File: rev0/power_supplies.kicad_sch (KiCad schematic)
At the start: 50 parts, among them IC1 ECP5-BGA256, U1 AP2171WG-7, U12 AP2171WG-7, U13 AP2171WG-7, U3 AP7366-33W5-7, U4 TCR2EF115, U5 MIC5504-2.5YM5

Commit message: hardware: use DNP field for DNP notation
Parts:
- TP28, TP29, TP3, TP30, TP31, TP4, TP5: DNP (none) -> DNP; Note DNP -> (none)
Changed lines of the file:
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@@
       (effects (font (size 1.27 1.27)) hide)
     )
-    (property "Note" "DNP" (id 4) (at 77.47 99.06 0)
+    (property "DNP" "DNP" (id 4) (at 77.47 99.06 0)
       (effects (font (size 1.27 1.27)) hide)
     )
@@
       (effects (font (size 1.27 1.27)) hide)
     )
-    (property "Note" "DNP" (id 4) (at 152.4 97.79 0)
+    (property "DNP" "DNP" (id 4) (at 152.4 97.79 0)
       (effects (font (size 1.27 1.27)) hide)
     )
@@
       (effects (font (size 1.27 1.27)) hide)
     )
-    (property "Note" "DNP" (id 4) (at 152.4 153.67 0)
+    (property "DNP" "DNP" (id 4) (at 152.4 153.67 0)
       (effects (font (size 1.27 1.27)) hide)
     )
@@
       (effects (font (size 1.27 1.27)) hide)
     )
-    (property "Note" "DNP" (id 4) (at 73.66 182.88 0)
+    (property "DNP" "DNP" (id 4) (at 73.66 182.88 0)
       (effects (font (size 1.27 1.27)) hide)
     )
@@
       (effects (font (size 1.27 1.27)) hide)
     )
-    (property "Note" "DNP" (id 4) (at 48.26 182.88 0)
+    (property "DNP" "DNP" (id 4) (at 48.26 182.88 0)
       (effects (font (size 1.27 1.27)) hide)
     )
@@
       (effects (font (size 1.27 1.27)) hide)
     )
-    (property "Note" "DNP" (id 4) (at 41.91 152.4 0)
+    (property "DNP" "DNP" (id 4) (at 41.91 152.4 0)
       (effects (font (size 1.27 1.27)) hide)
     )
@@
       (effects (font (size 1.27 1.27)) hide)
     )
-    (property "Note" "DNP" (id 4) (at 58.42 152.4 0)
-      (effects (font (size 1.27 1.27)) hide)
-    )
+    (property "DNP" "DNP" (id 4) (at 58.42 152.4 0)
+      (effects (font (size 1.27 1.27)) hide)
+    )

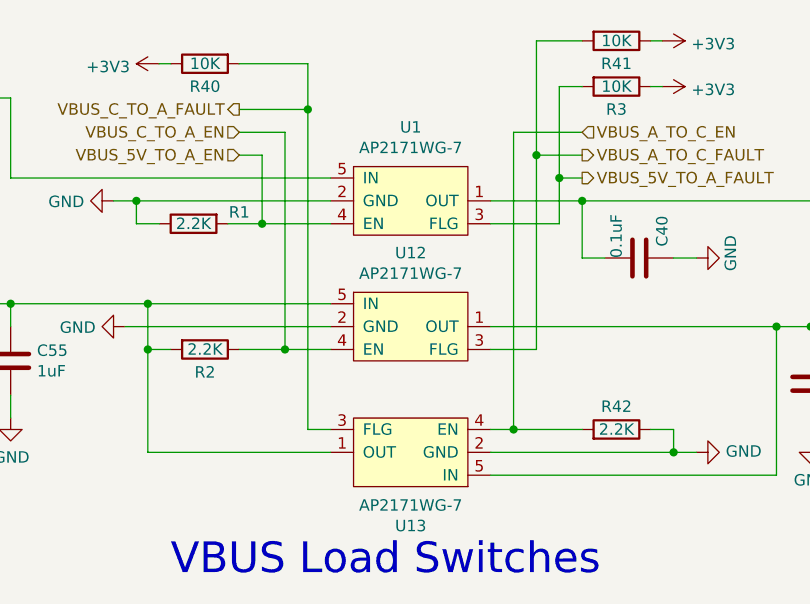
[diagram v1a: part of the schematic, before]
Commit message: hardware: consistently use lowercase k for kilo
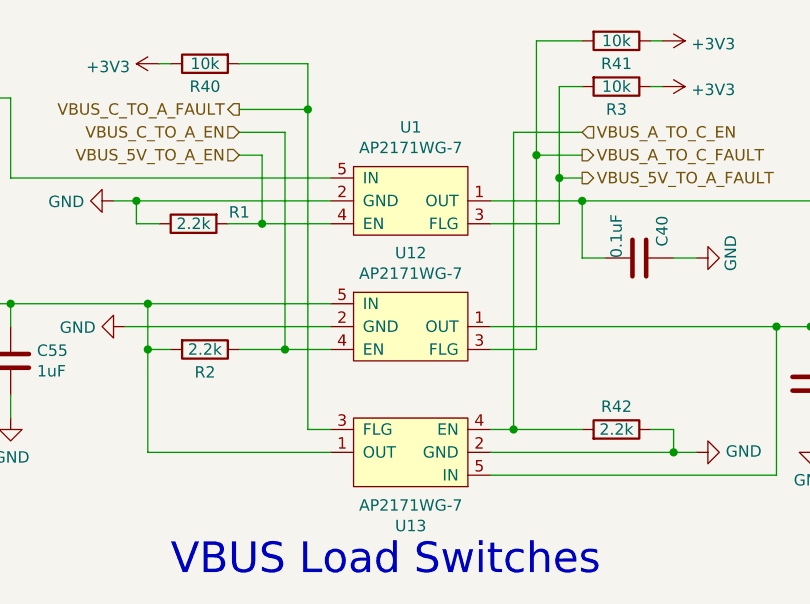
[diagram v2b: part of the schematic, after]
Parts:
- R1, R2, R42: value 2.2K -> 2.2k
- R3, R40, R41: value 10K -> 10k
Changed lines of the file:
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@@
     (in_bom yes) (on_board yes)
     (property "Reference" "R2" (id 0) (at 184.15 52.07 90))
-    (property "Value" "2.2K" (id 1) (at 184.15 49.53 90))
+    (property "Value" "2.2k" (id 1) (at 184.15 49.53 90))
     (property "Footprint" "Resistor_SMD:R_0402_1005Metric" (id 2) (at 184.15 47.752 90)
       (effects (font (size 1.27 1.27)) hide)
@@
     (in_bom yes) (on_board yes)
     (property "Reference" "R1" (id 0) (at 187.96 34.29 90))
-    (property "Value" "2.2K" (id 1) (at 182.88 35.56 90))
+    (property "Value" "2.2k" (id 1) (at 182.88 35.56 90))
     (property "Footprint" "Resistor_SMD:R_0402_1005Metric" (id 2) (at 182.88 33.782 90)
       (effects (font (size 1.27 1.27)) hide)
@@
     (in_bom yes) (on_board yes)
     (property "Reference" "R42" (id 0) (at 229.87 55.88 90))
-    (property "Value" "2.2K" (id 1) (at 229.87 58.42 90))
+    (property "Value" "2.2k" (id 1) (at 229.87 58.42 90))
     (property "Footprint" "Resistor_SMD:R_0402_1005Metric" (id 2) (at 229.87 60.198 90)
       (effects (font (size 1.27 1.27)) hide)
@@
     (in_bom yes) (on_board yes)
     (property "Reference" "R3" (id 0) (at 229.87 22.86 90))
-    (property "Value" "10K" (id 1) (at 229.87 20.32 90))
+    (property "Value" "10k" (id 1) (at 229.87 20.32 90))
     (property "Footprint" "Resistor_SMD:R_0402_1005Metric" (id 2) (at 229.87 18.542 90)
       (effects (font (size 1.27 1.27)) hide)
@@
     (in_bom yes) (on_board yes)
     (property "Reference" "R41" (id 0) (at 229.87 17.78 90))
-    (property "Value" "10K" (id 1) (at 229.87 15.24 90))
+    (property "Value" "10k" (id 1) (at 229.87 15.24 90))
     (property "Footprint" "Resistor_SMD:R_0402_1005Metric" (id 2) (at 229.87 13.462 90)
       (effects (font (size 1.27 1.27)) hide)
@@
     (in_bom yes) (on_board yes)
     (property "Reference" "R40" (id 0) (at 184.15 20.32 90))
-    (property "Value" "10K" (id 1) (at 184.15 17.78 90))
+    (property "Value" "10k" (id 1) (at 184.15 17.78 90))
     (property "Footprint" "Resistor_SMD:R_0402_1005Metric" (id 2) (at 184.15 16.002 90)
       (effects (font (size 1.27 1.27)) hide)

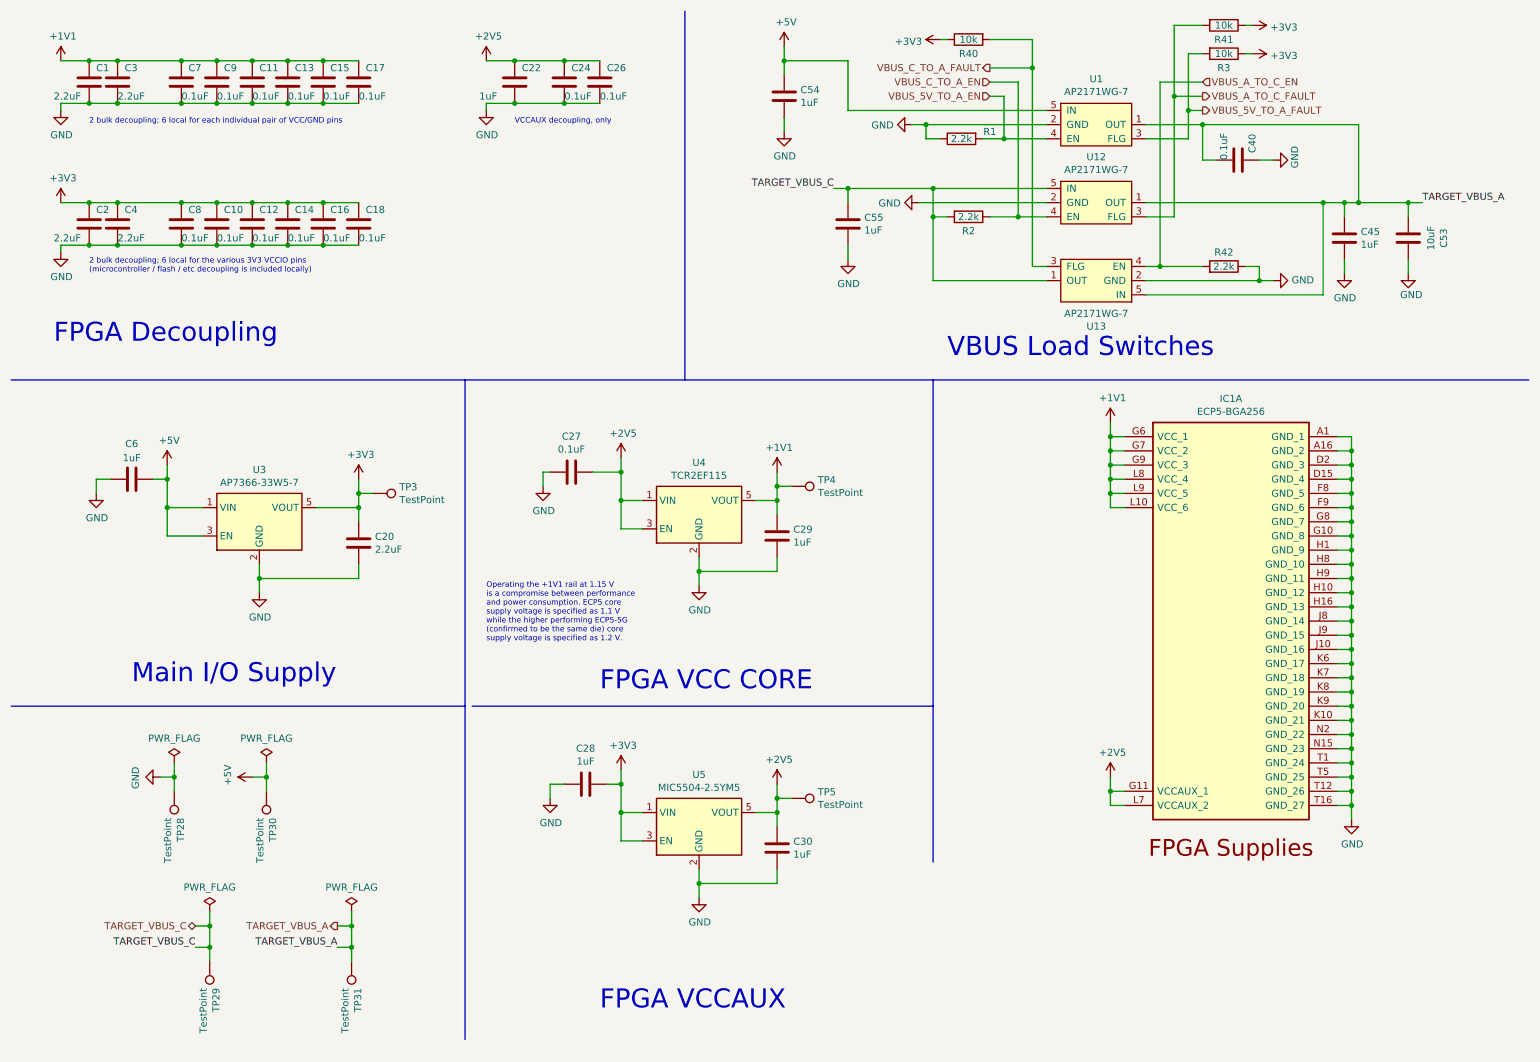
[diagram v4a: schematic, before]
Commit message: hardware: restore 1.8 V RAM supply as an option
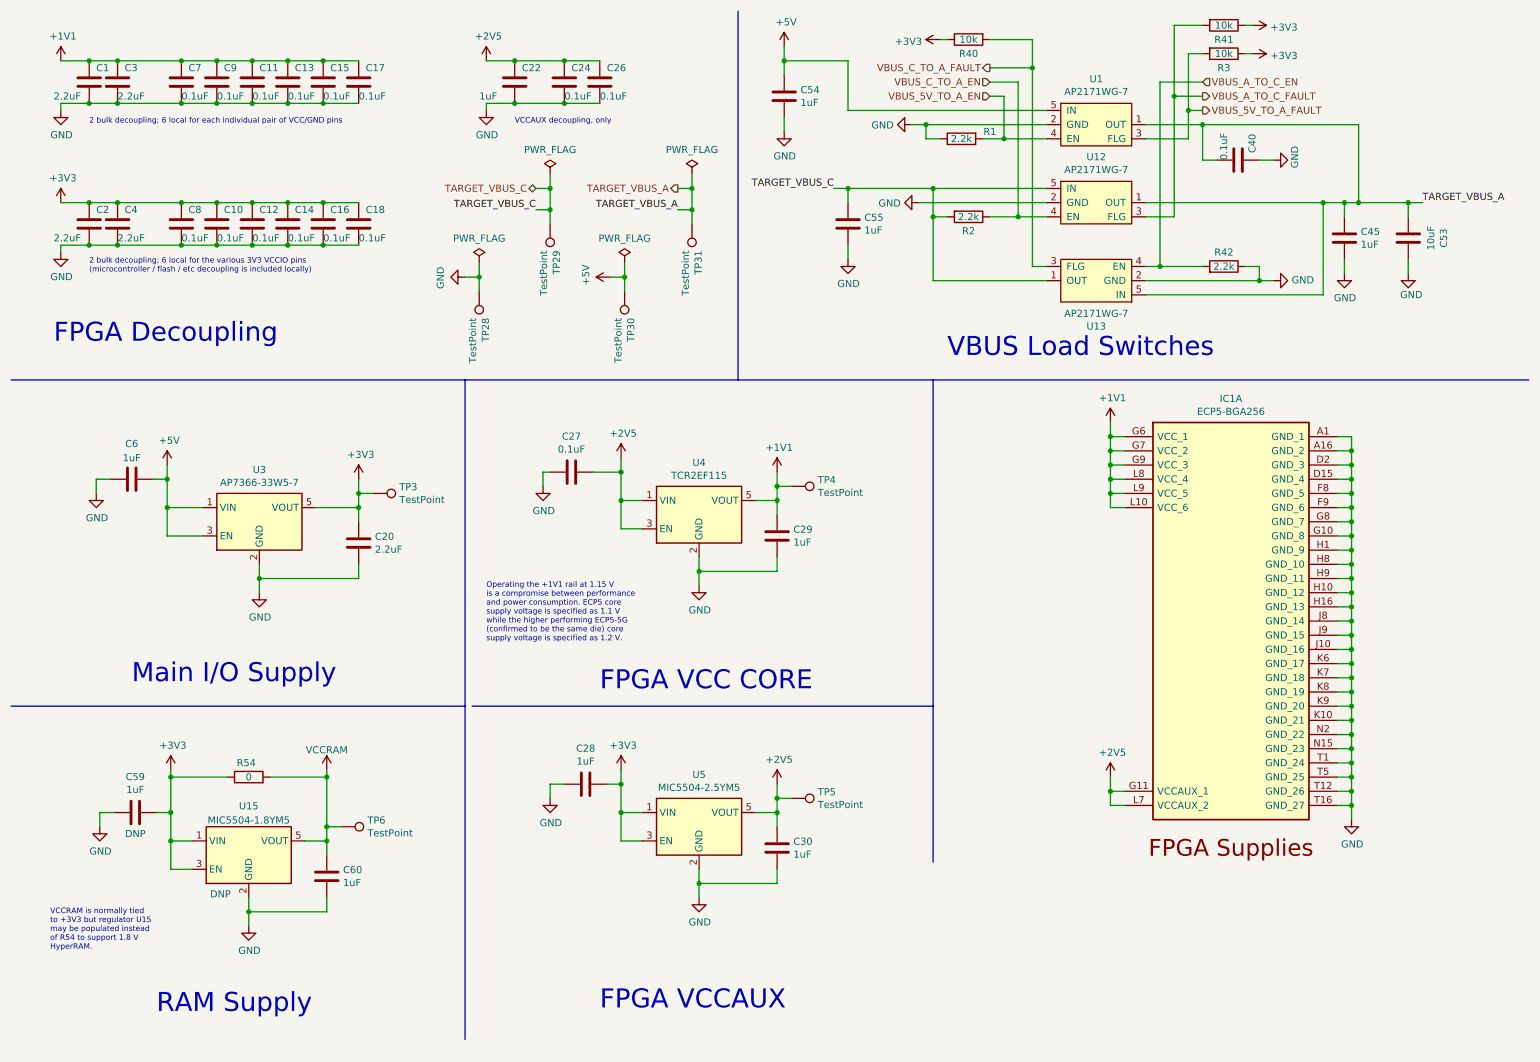
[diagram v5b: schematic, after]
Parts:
- added C59, C60: 1uF, Capacitor_SMD:C_0603_1608Metric, symbol Device:C
- added R54: 0, Resistor_SMD:R_0402_1005Metric, symbol Device:R
- added TP6: TestPoint, TestPoint:TestPoint_Pad_D1.0mm, symbol Connector:TestPoint
- added U15: MIC5504-1.8YM5, Package_TO_SOT_SMD:SOT-23-5, symbol Regulator_Linear:MIC5504-1.8YM5
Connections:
- net +3V3: now also C59.1, R54.1, U15.1 (VIN), U15.3 (EN)
- net GND: now also C59.2, C60.2, U15.2 (GND)
- new net VCCRAM: C60.1, R54.2, TP6.1, U15.5 (VOUT)
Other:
- note added: "RAM Supply"
- note added: "VCCRAM is normally tied to +3V3 but regulator U15 may be populated instead of R54 to support 1.8 V HyperRAM."
- moved on the sheet: TP28, TP29, TP30, TP31

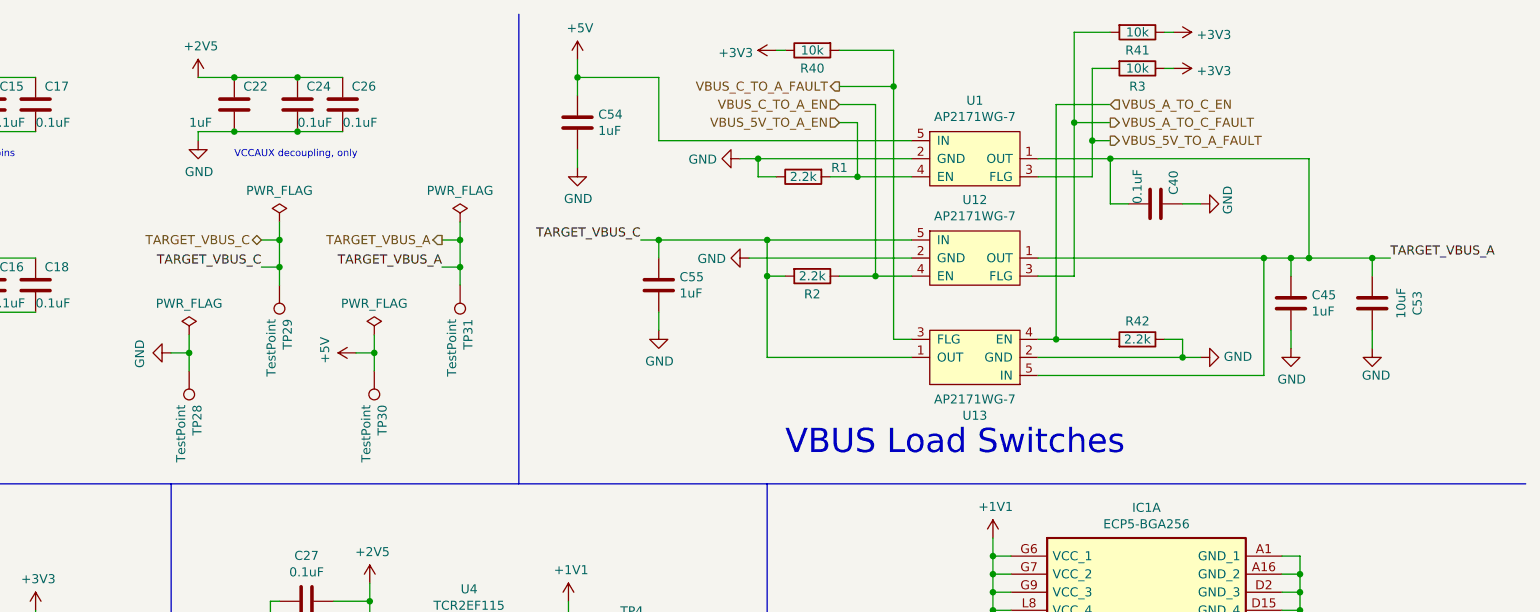
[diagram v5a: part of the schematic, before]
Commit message: hardware: replace VBUS pass-through switches
- increase maximum voltage with discrete FET solution
- pass through Control and Aux VBUS directly, not +5V supply rail
- add current sense resistors
- eliminate discharge current of previous power switches
- eliminate possible overvoltage condition of previous power switches
- remove 10 uF VBUS output capacitor C53
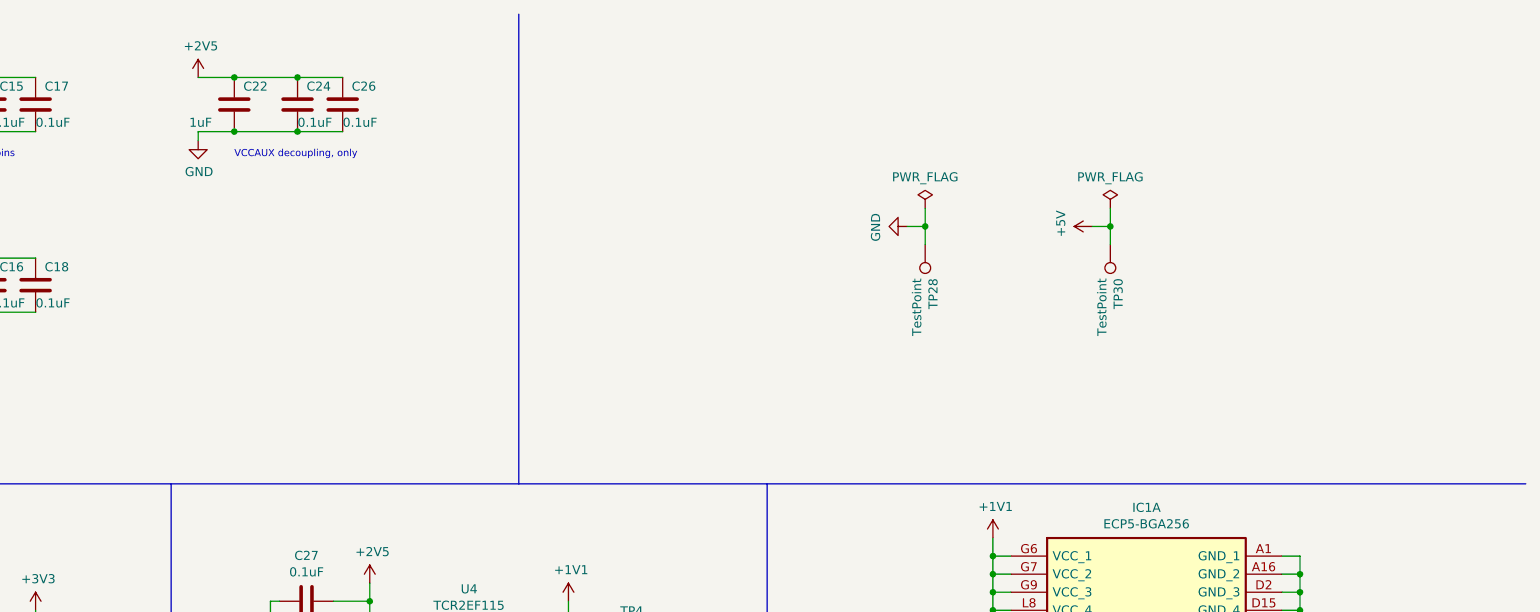
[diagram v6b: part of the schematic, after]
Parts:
- removed C40: 0.1uF, Capacitor_SMD:C_0402_1005Metric, symbol Device:C
- removed C45, C54, C55: 1uF, Capacitor_SMD:C_0603_1608Metric, symbol Device:C
- removed C53: 10uF, Capacitor_SMD:C_0805_2012Metric, symbol Device:C
- removed R1, R2, R42: 2.2k, Resistor_SMD:R_0402_1005Metric, symbol Device:R
- removed R3, R40, R41: 10k, Resistor_SMD:R_0402_1005Metric, symbol Device:R
- removed TP29, TP31: TestPoint, TestPoint:TestPoint_Pad_D1.0mm, symbol Connector:TestPoint
- removed U1, U12, U13: AP2171WG-7, Package_TO_SOT_SMD:SOT-23-5, symbol support_hardware:AP22804-SOT
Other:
- note removed: "VBUS Load Switches"
- moved on the sheet: TP28, TP30

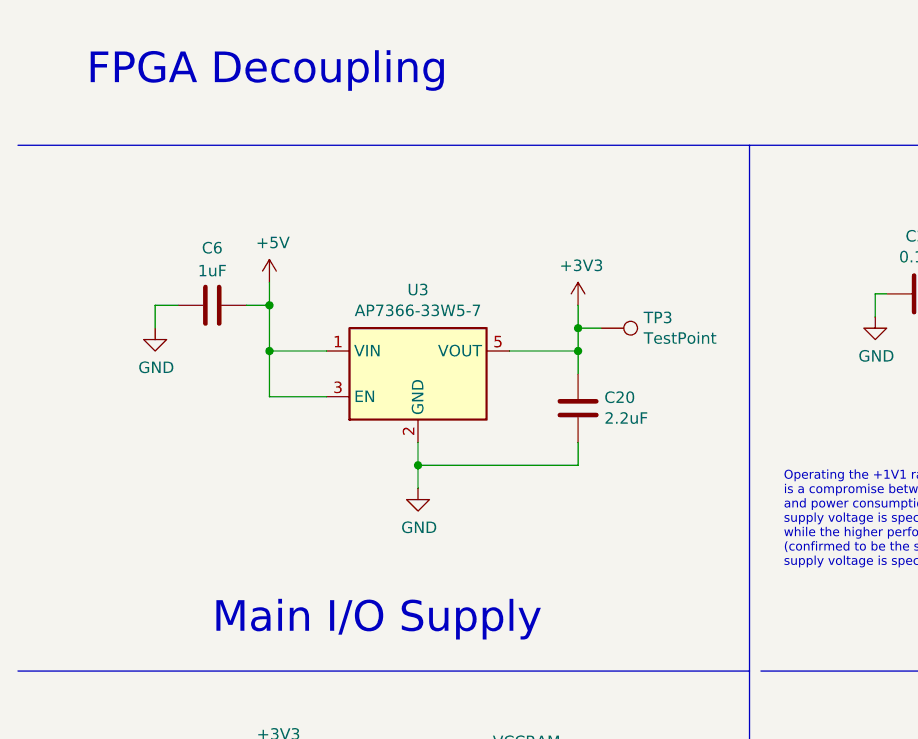
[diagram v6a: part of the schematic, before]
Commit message: hardware: replace +3V3 regulator U3
- support higher current
- improve heat dissipation
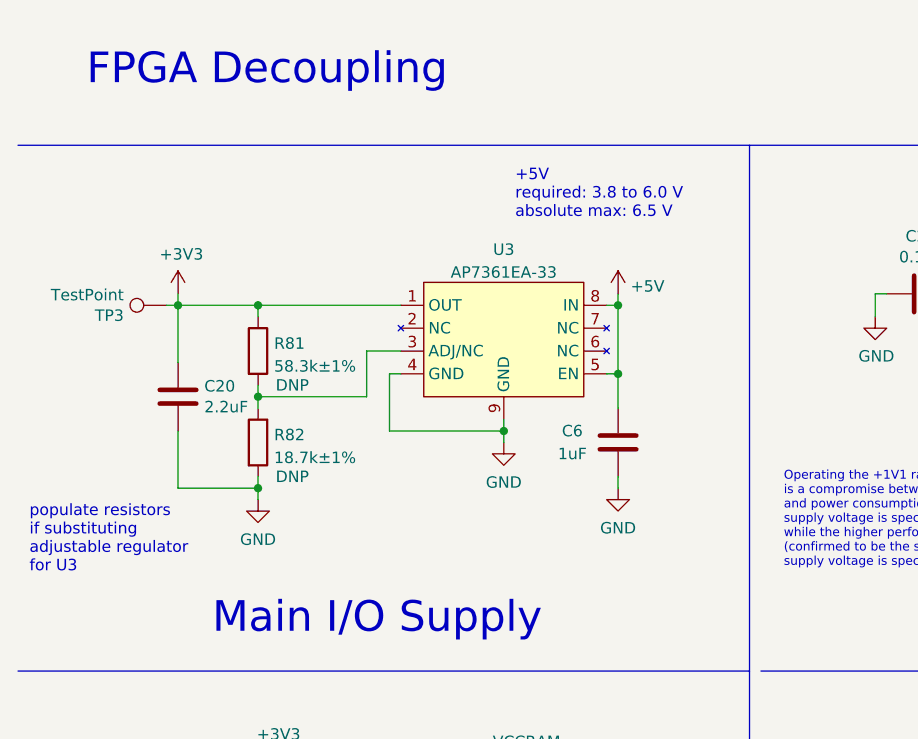
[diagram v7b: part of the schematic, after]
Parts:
- removed U3: AP7366-33W5-7, Package_TO_SOT_SMD:SOT-23-5, symbol Regulator_Linear:MIC5504-1.8YM5
- added R81: 58.3k±1%, Resistor_SMD:R_0402_1005Metric, symbol Device:R
- added R82: 18.7k±1%, Resistor_SMD:R_0402_1005Metric, symbol Device:R
- added U3: AP7361EA-33, Package_DFN_QFN:DFN-8-1EP_3x3mm_P0.65mm_EP1.55x2.4mm, symbol support_hardware:AP7361EA-XXFGE-7
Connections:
- net +3V3: now also R81.1, U3.1 (OUT)
- net +5V: now also U3.5 (EN), U3.8 (IN)
- net GND: now also R82.2, U3.4 (GND), U3.9 (GND)
- new net: R81.2, R82.1, U3.3 (ADJ/NC)
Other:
- note added: "+5V required: 3.8 to 6.0 V absolute max: 6.5 V"
- note added: "populate resistors if substituting adjustable regulator for U3"
- moved on the sheet: C20, C6, TP3
